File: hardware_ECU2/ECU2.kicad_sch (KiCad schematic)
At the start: 7 parts, among them J1 capacitive conector, J2 indutivo_conector, J6 sensor velocidade, U1 ESP32-WROOM-32

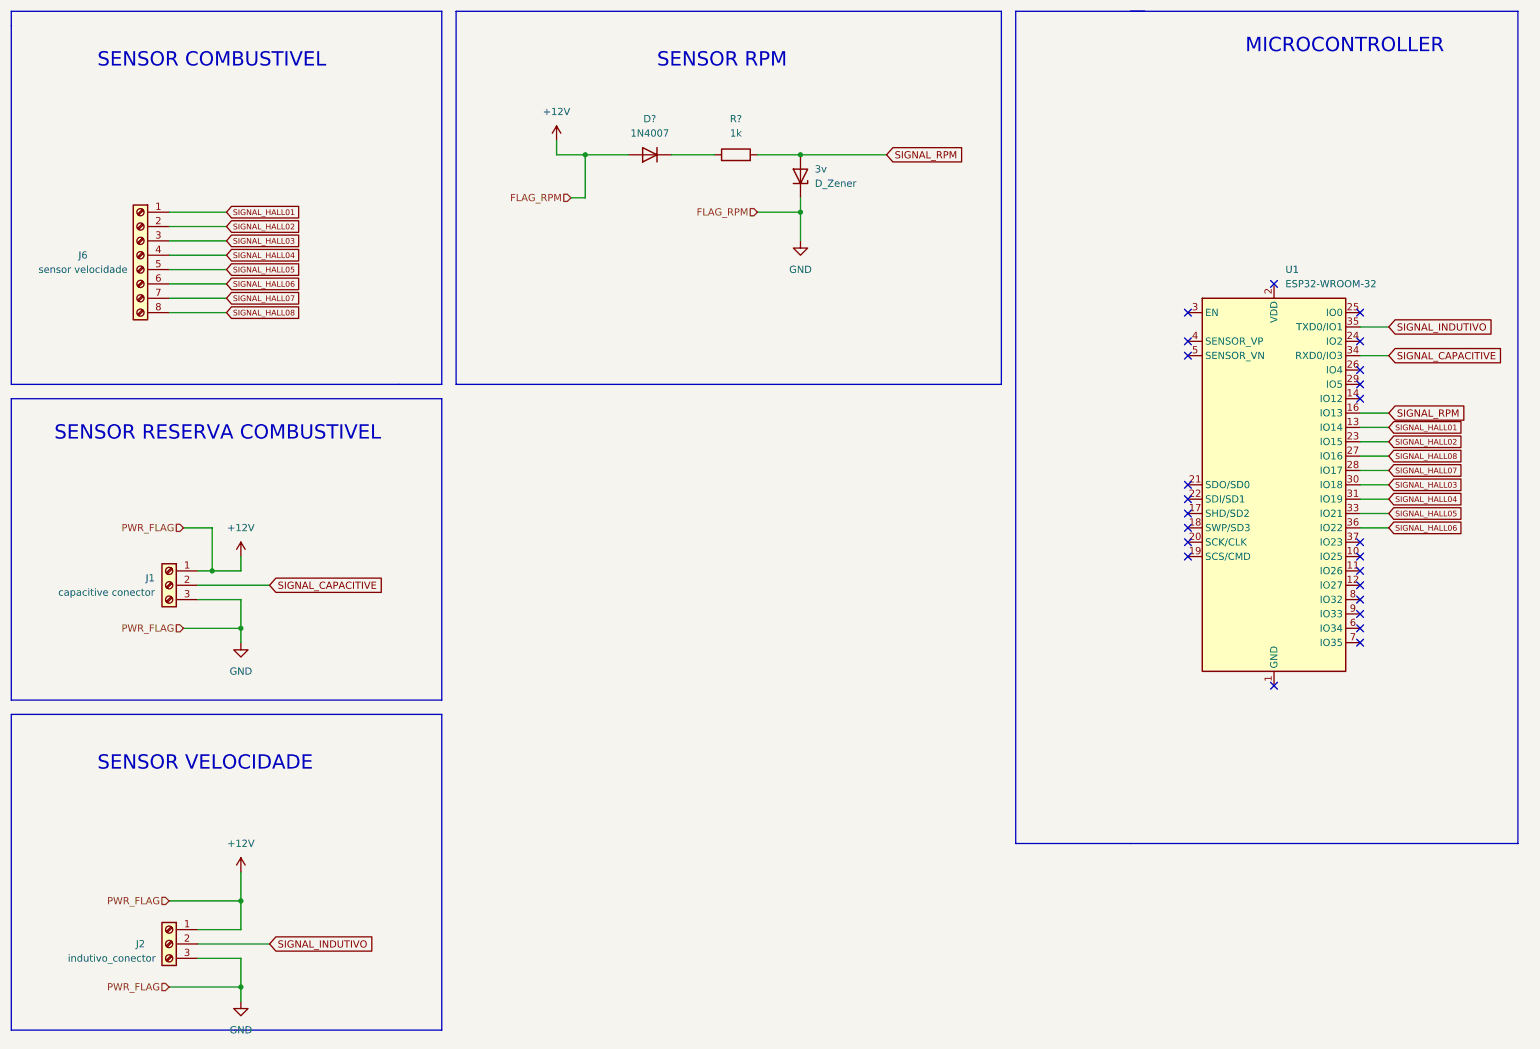
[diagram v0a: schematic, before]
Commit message: fiz pwr_flag and add caps
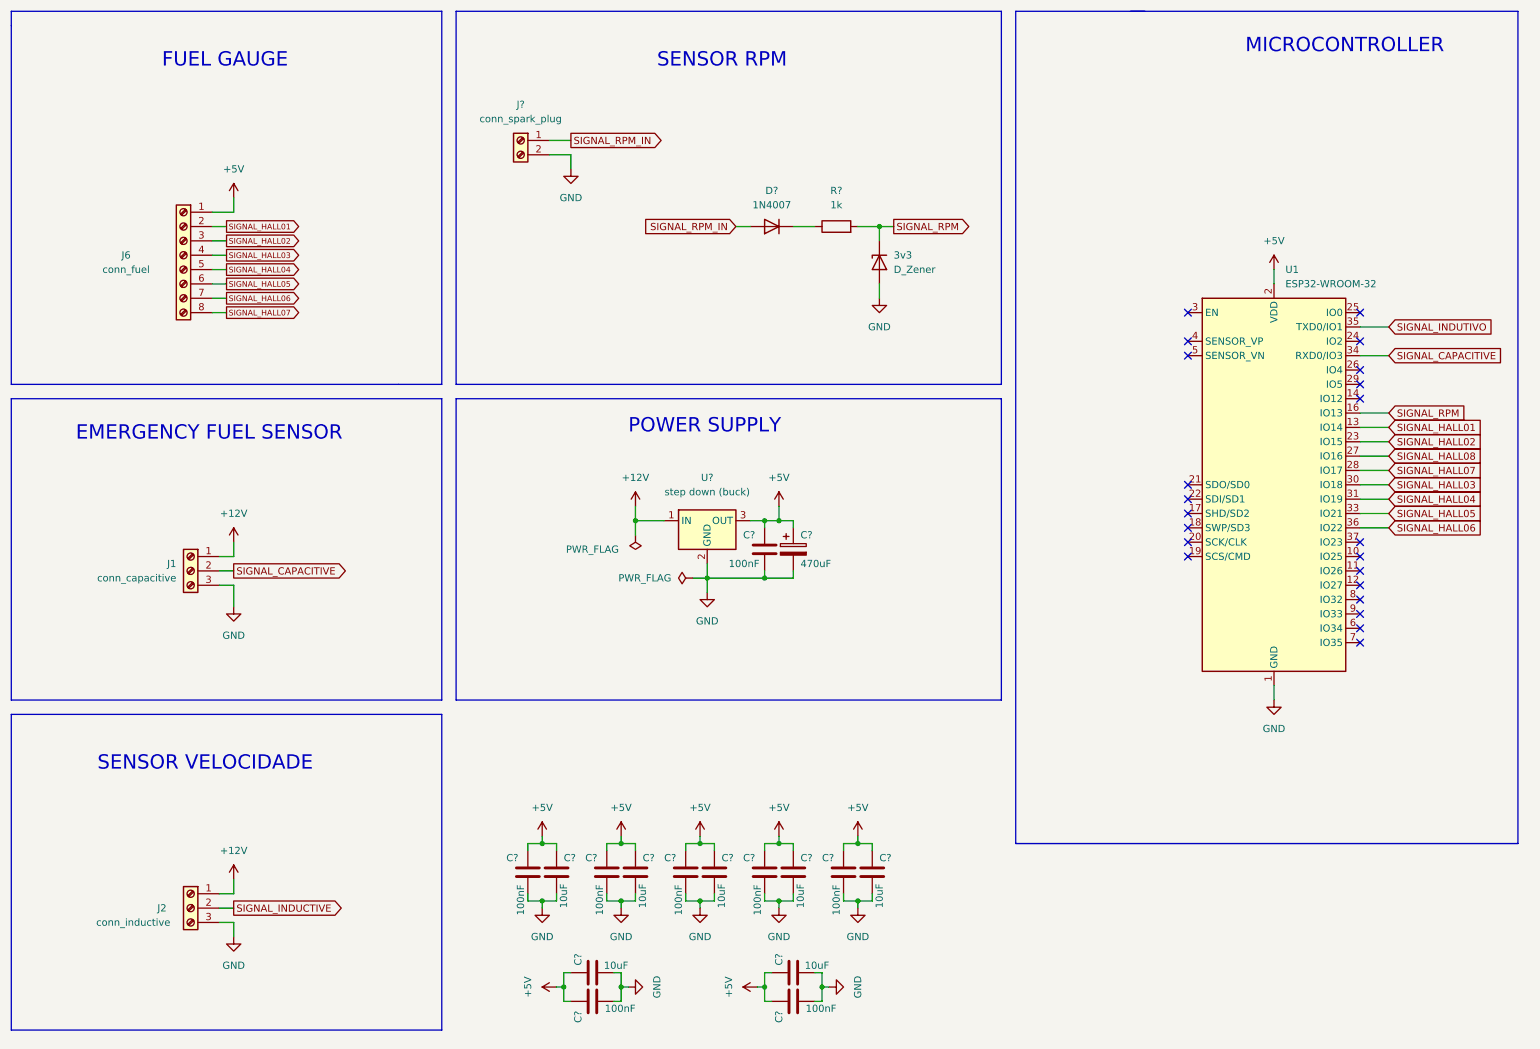
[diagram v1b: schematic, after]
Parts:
- added C? (x8): 100nF, symbol Device:C
- added C? (x7): 10uF, symbol Device:C
- added C?: 470uF, symbol Device:C_Polarized
- added J?: conn_spark_plug, symbol Connector:Screw_Terminal_01x02
- added U?: step down (buck), Converter_DCDC:Converter_DCDC_Murata_OKI-78SR_Vertical, symbol Converter_DCDC:OKI-78SR-3.3_1.5-W36-C
- J1: value capacitive conector -> conn_capacitive
- J2: value indutivo_conector -> conn_inductive
- J6: value sensor velocidade -> conn_fuel
- renumbered 3v to 3v3
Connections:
- net SIGNAL_HALL01: now also J6.2 (Pin_2); no longer J6.1 (Pin_1)
- net SIGNAL_HALL02: now also J6.3 (Pin_3); no longer J6.2 (Pin_2)
- net SIGNAL_HALL03: now also J6.4 (Pin_4); no longer J6.3 (Pin_3)
- net SIGNAL_HALL04: now also J6.5 (Pin_5); no longer J6.4 (Pin_4)
- net SIGNAL_HALL05: now also J6.6 (Pin_6); no longer J6.5 (Pin_5)
- net SIGNAL_HALL06: now also J6.7 (Pin_7); no longer J6.6 (Pin_6)
- net SIGNAL_HALL07: now also J6.8 (Pin_8); no longer J6.7 (Pin_7)
- net SIGNAL_HALL08: no longer J6.8 (Pin_8)
- net SIGNAL_INDUTIVO: no longer J2.2 (Pin_2)
- net SIGNAL_RPM: now also 3v3.1 (K); no longer 3v3.2 (A)
- net GND: now reaches U1.1 (GND), U1.15 (GND), U1.38 (GND), U1.39 (GND)
- net GND: now also 3v3.2 (A), J1.3 (Pin_3), J2.3 (Pin_3), C?.2, C?.2, C?.2, C?.2, C?.2, C?.2, C?.2, C?.2, C?.2, C?.2, C?.2, C?.2, C?.2, C?.2, C?.2, C?.2, J?.2 (Pin_2), U?.2 (GND)
- net +5V: now reaches U1.2 (VDD)
- net +5V: now also J6.1 (Pin_1), C?.1, C?.1, C?.1, C?.1, C?.1, C?.1, C?.1, C?.1, C?.1, C?.1, C?.1, C?.1, C?.1, C?.1, C?.1, C?.1, U?.3 (OUT)
- net FLAG_RPM renamed SIGNAL_RPM_IN
- net SIGNAL_RPM_IN: now also J?.1 (Pin_1); no longer 3v3.1 (K)
- net PWR_FLAG renamed +12V
- net +12V: now also U?.1 (IN); no longer J1.3 (Pin_3), J2.3 (Pin_3)
- new net SIGNAL_INDUCTIVE: J2.2 (Pin_2)
- no-connect marks 24 -> 22
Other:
- note added: "EMERGENCY FUEL SENSOR"
- note added: "FUEL GAUGE"
- note added: "POWER SUPPLY"
- note removed: "SENSOR COMBUSTIVEL"
- note removed: "SENSOR RESERVA COMBUSTIVEL"
- moved on the sheet: 3v3, D?, J1, J2, J6, R?

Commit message: fix pin position
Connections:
- net SIGNAL_CAPACITIVE: now also U1.27 (IO16); no longer U1.34 (RXD0/IO3)
- net SIGNAL_HALL01: now also U1.11 (IO26); no longer U1.13 (IO14)
- net SIGNAL_HALL02: now also U1.12 (IO27); no longer U1.23 (IO15)
- net SIGNAL_HALL03: now also U1.6 (IO34); no longer U1.30 (IO18)
- net SIGNAL_HALL04: now also U1.7 (IO35); no longer U1.31 (IO19)
- net SIGNAL_HALL05: now also U1.4 (SENSOR_VP); no longer U1.33 (IO21)
- net SIGNAL_HALL06: now also U1.5 (SENSOR_VN); no longer U1.36 (IO22)
- net SIGNAL_HALL07: now also U1.9 (IO33); no longer U1.28 (IO17)
- net SIGNAL_HALL08: now also U1.8 (IO32); no longer U1.27 (IO16)
- net SIGNAL_INDUTIVO: now also U1.28 (IO17); no longer U1.35 (TXD0/IO1)
- net SIGNAL_RPM: now also U1.26 (IO4); no longer U1.16 (IO13)
- no-connect marks 22 -> 11

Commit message: Update ECU2.kicad_sch
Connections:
- net SIGNAL_INDUTIVO is gone; now on net SIGNAL_INDUCTIVE: U1.28 (IO17)
- net SIGNAL_RPM renamed SIGNAL_RPM_OUT
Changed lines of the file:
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@@
     )
   )
-  (global_label "SIGNAL_RPM" (shape output) (at 171.45 53.34 0) (fields_autoplaced)
+  (global_label "SIGNAL_RPM_OUT" (shape output) (at 171.45 53.34 0) (fields_autoplaced)
     (effects (font (size 1.27 1.27)) (justify left))
-    (property "Referências entre as folhas" "${INTERSHEET_REFS}" (id 0) (at 185.3536 53.2606 0)
+    (property "Referências entre as folhas" "${INTERSHEET_REFS}" (id 0) (at 189.9498 53.2606 0)
       (effects (font (size 1.27 1.27)) (justify left) hide)
     )
@@
     )
   )
-  (global_label "SIGNAL_RPM" (shape input) (at 259.08 78.74 0) (fields_autoplaced)
+  (global_label "SIGNAL_RPM_OUT" (shape input) (at 259.08 78.74 0) (fields_autoplaced)
     (effects (font (size 1.27 1.27)) (justify left))
-    (property "Referências entre as folhas" "${INTERSHEET_REFS}" (id 0) (at 272.9836 78.6606 0)
+    (property "Referências entre as folhas" "${INTERSHEET_REFS}" (id 0) (at 277.5798 78.6606 0)
       (effects (font (size 1.27 1.27)) (justify left) hide)
     )
@@
     )
   )
-  (global_label "SIGNAL_INDUTIVO" (shape input) (at 259.08 96.52 0) (fields_autoplaced)
+  (global_label "SIGNAL_INDUCTIVE" (shape input) (at 259.08 96.52 0) (fields_autoplaced)
     (effects (font (size 1.27 1.27)) (justify left))
-    (property "Referências entre as folhas" "${INTERSHEET_REFS}" (id 0) (at 277.5193 96.4406 0)
+    (property "Referências entre as folhas" "${INTERSHEET_REFS}" (id 0) (at 278.6079 96.4406 0)
       (effects (font (size 1.27 1.27)) (justify left) hide)
     )

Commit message: Update ECU2.kicad_sch
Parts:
- D2: renamed from 3v3; value D_Zener -> zener_3v3
- gave numbers to parts that had none: 20
- renumbered J6 to J1, J1 to J2, J2 to J3, U1 to U2
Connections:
- net SIGNAL_HALL08: no longer names the net of U2.8 (IO32)
- no-connect marks 11 -> 23
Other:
- moved on the sheet: D1, D2, R1

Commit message: fix hall pins connections
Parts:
- removed J1: conn_fuel, symbol Connector:Screw_Terminal_01x08
- removed J2: conn_capacitive, symbol Connector:Screw_Terminal_01x03
- removed J3: conn_inductive, symbol Connector:Screw_Terminal_01x03
- removed J4: conn_spark_plug, symbol Connector:Screw_Terminal_01x02
- added C1, C2: 10nF(103), symbol Device:C
- added D1, D2: 3V3, symbol Device:D_Zener
- added J1: Conn_fuel, symbol Connector:Conn_01x03_Male
- added J2: Conn_speed, symbol Connector:Conn_01x03_Male
- added J3: Conn_fuel_gauge, symbol Connector:Conn_01x08_Male
- added J4: Conn_RPM, symbol Connector:Conn_01x01_Male
- added R1, R2: 5k1, symbol Device:R
- renumbered C8 to C10, C9 to C11, C10 to C12, C11 to C13, C12 to C14, C13 to C15, C14 to C16, C15 to C17, C16 to C18, C1 to C3, C2 to C4, C3 to C5, C4 to C6, C5 to C7, C6 to C8, C7 to C9, D1 to D3, D2 to D4, R1 to R3
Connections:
- net SIGNAL_HALL07 is gone; now on net SIGNAL_HALL03: U2.9 (IO33)
- net +12V: now also J1.1 (Pin_1), J2.1 (Pin_1)
- net +5V: now also J3.1 (Pin_1)
- net GND: now also C1.2, C2.2, D1.2 (A), D2.2 (A), J1.3 (Pin_3), J2.3 (Pin_3), J3.8 (Pin_8)
- net SIGNAL_CAPACITIVE: now also C1.1, D1.1 (K), R1.2
- net SIGNAL_HALL01: now also J3.2 (Pin_2)
- net SIGNAL_HALL02: now also U2.10 (IO25), J3.3 (Pin_3); no longer U2.12 (IO27)
- net SIGNAL_HALL03: now also J3.4 (Pin_4); no longer U2.6 (IO34)
- net SIGNAL_HALL04: now also U2.8 (IO32), J3.5 (Pin_5); no longer U2.7 (IO35)
- net SIGNAL_HALL05: now also U2.7 (IO35), J3.6 (Pin_6); no longer U2.4 (SENSOR_VP)
- net SIGNAL_HALL06: now also U2.6 (IO34), J3.7 (Pin_7); no longer U2.5 (SENSOR_VN)
- net SIGNAL_INDUCTIVE: now also C2.1, D2.1 (K), R2.2
- net SIGNAL_RPM_IN: no longer names the net of D3.2 (A)
- net SIGNAL_RPM_IN: now also J4.1 (Pin_1)
- net SIGNAL_RPM_OUT renamed SIGNAL_RPM
- new net: J1.2 (Pin_2), R1.1
- new net: J2.2 (Pin_2), R2.1
- no-connect marks 23 -> 24
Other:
- moved on the sheet: D3, D4, R3
